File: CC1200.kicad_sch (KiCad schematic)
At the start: 55 parts, among them U3 CC1200, U4 MCP6001-OT, X1 40MHz

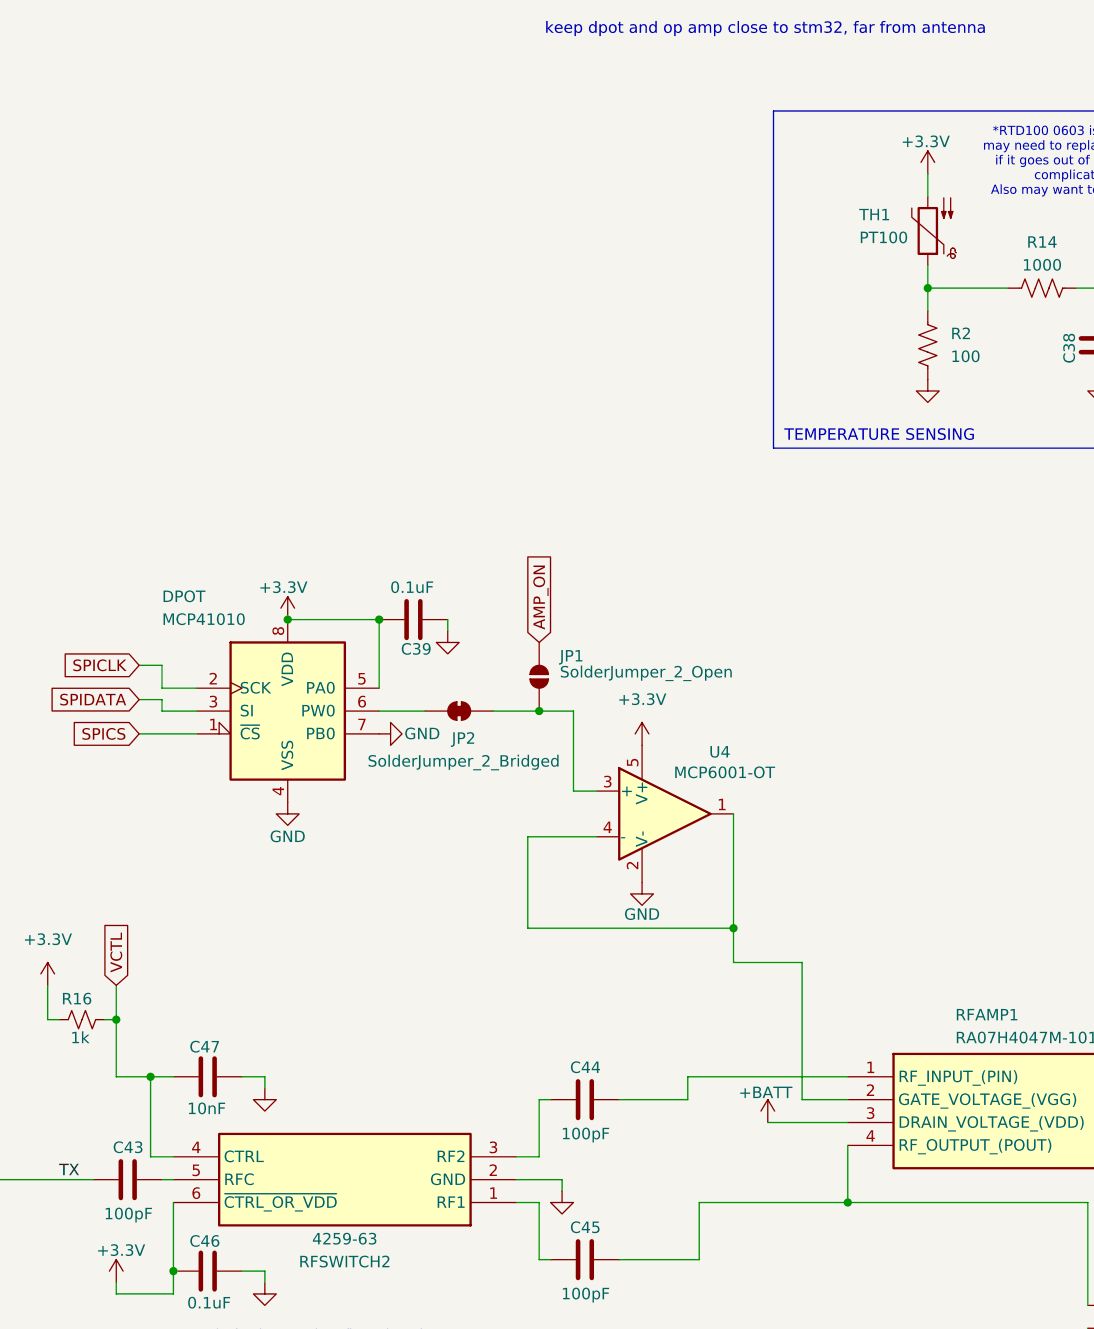
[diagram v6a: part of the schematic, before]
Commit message: reference/backup for mostly routed pcb
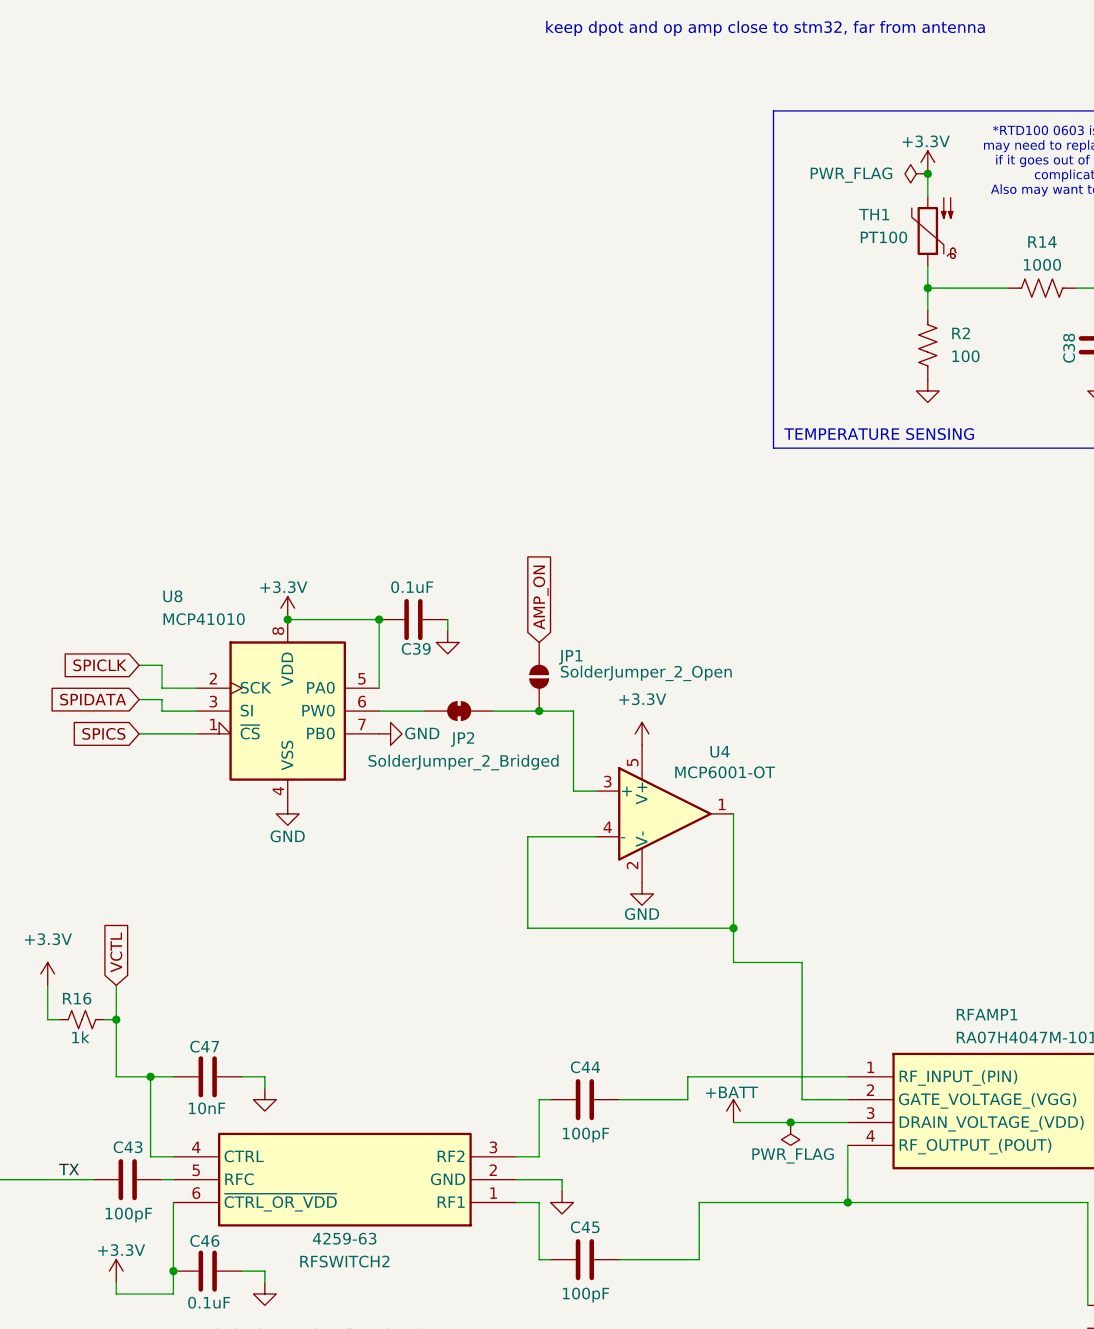
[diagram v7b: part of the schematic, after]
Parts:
- AE1: footprint (none) -> Connector_Coaxial:SMA_BAT_Wireless_BWSMA-KWE-Z001; LCSC (none) -> C7498154
- JP1: footprint (none) -> Jumper:SolderJumper-2_P1.3mm_Open_RoundedPad1.0x1.5mm
- JP2: footprint (none) -> Jumper:SolderJumper-2_P1.3mm_Bridged_RoundedPad1.0x1.5mm
- RFAMP1: footprint RA07H4047M:RA07H4047M101 -> RA07H4047M:RA07H4047M101_HORIZ
- U8: renamed from DPOT; footprint (none) -> MCP41010:SOIC127P599X175-8N; LCSC (none) -> C136395
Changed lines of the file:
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@@
 	)
 	(junction
+		(at 346.71 142.24)
+		(diameter 0)
+		(color 0 0 0 0)
+	)
+	(junction
 		(at 166.37 148.59)
 		(diameter 0)
@@
 	)
 	(junction
+		(at 361.95 36.83)
+		(diameter 0)
+		(color 0 0 0 0)
+	)
+	(junction
 		(at 300.99 86.36)
 		(diameter 0)
@@
 	(wire
 		(pts
-			(xy 344.17 142.24) (xy 353.06 142.24)
+			(xy 340.36 142.24) (xy 346.71 142.24)
 		)
 		(stroke
@@
 	(wire
 		(pts
+			(xy 346.71 142.24) (xy 353.06 142.24)
+		)
+		(stroke
+			(width 0)
+			(type default)
+		)
+	)
+	(wire
+		(pts
 			(xy 228.6 140.97) (xy 228.6 148.59)
 		)
@@
 		(on_board yes)
 		(dnp no)
-		(property "Reference" "DPOT"
+		(property "Reference" "U8"
 			(at 276.86 83.82 0)
 			(effects
@@
 			)
 		)
-		(property "Footprint" ""
+		(property "Footprint" "MCP41010:SOIC127P599X175-8N"
 			(at 290.83 96.52 0)
 			(effects
@@
 			)
 		)
+		(property "LCSC" "C136395"
+			(at 290.83 96.52 0)
+			(effects
+				(font
+					(size 1.27 1.27)
+				)
+				(hide yes)
+			)
+		)
 		(pin "2"
 		)
@@
 			(project ""
 				(path "/4108571e-8c4c-4eba-a51f-04b21c4cec35/dfcafdf4-f213-4518-865d-ab9ee2b88e54"
-					(reference "DPOT")
+					(reference "U8")
 					(unit 1)
 				)
@@
 	)
 	(symbol
+		(lib_id "power:PWR_FLAG")
+		(at 361.95 36.83 90)
+		(unit 1)
+		(exclude_from_sim no)
+		(in_bom yes)
+		(on_board yes)
+		(dnp no)
+		(fields_autoplaced yes)
+		(property "Reference" "#FLG05"
+			(at 360.045 36.83 0)
+			(effects
+				(font
+					(size 1.27 1.27)
+				)
+				(hide yes)
+			)
+		)
+		(property "Value" "PWR_FLAG"
+			(at 358.14 36.8299 90)
+			(effects
+				(font
+					(size 1.27 1.27)
+				)
+				(justify left)
+			)
+		)
+		(property "Footprint" ""
+			(at 361.95 36.83 0)
+			(effects
+				(font
+					(size 1.27 1.27)
+				)
+				(hide yes)
+			)
+		)
+		(property "Datasheet" "~"
+			(at 361.95 36.83 0)
+			(effects
+				(font
+					(size 1.27 1.27)
+				)
+				(hide yes)
+			)
+		)
+		(property "Description" "Special symbol for telling ERC where power comes from"
+			(at 361.95 36.83 0)
+			(effects
+				(font
+					(size 1.27 1.27)
+				)
+				(hide yes)
+			)
+		)
+		(pin "1"
+		)
+		(instances
+			(project ""
+				(path "/4108571e-8c4c-4eba-a51f-04b21c4cec35/dfcafdf4-f213-4518-865d-ab9ee2b88e54"
+					(reference "#FLG05")
+					(unit 1)
+				)
+			)
+		)
+	)
+	(symbol
 		(lib_id "power:GND")
 		(at 125.73 113.03 0)
@@
 	)
 	(symbol
+		(lib_id "power:PWR_FLAG")
+		(at 346.71 142.24 180)
+		(unit 1)
+		(exclude_from_sim no)
+		(in_bom yes)
+		(on_board yes)
+		(dnp no)
+		(property "Reference" "#FLG04"
+			(at 346.71 144.145 0)
+			(effects
+				(font
+					(size 1.27 1.27)
+				)
+				(hide yes)
+			)
+		)
+		(property "Value" "PWR_FLAG"
+			(at 346.964 145.796 0)
+			(effects
+				(font
+					(size 1.27 1.27)
+				)
+			)
+		)
+		(property "Footprint" ""
+			(at 346.71 142.24 0)
+			(effects
+				(font
+					(size 1.27 1.27)
+				)
+				(hide yes)
+			)
+		)
+		(property "Datasheet" "~"
+			(at 346.71 142.24 0)
+			(effects
+				(font
+					(size 1.27 1.27)
+				)
+				(hide yes)
+			)
+		)
+		(property "Description" "Special symbol for telling ERC where power comes from"
+			(at 346.71 142.24 0)
+			(effects
+				(font
+					(size 1.27 1.27)
+				)
+				(hide yes)
+			)
+		)
+		(pin "1"
+		)
+		(instances
+			(project ""
+				(path "/4108571e-8c4c-4eba-a51f-04b21c4cec35/dfcafdf4-f213-4518-865d-ab9ee2b88e54"
+					(reference "#FLG04")
+					(unit 1)
+				)
+			)
+		)
+	)
+	(symbol
 		(lib_id "power:GND")
 		(at 168.91 91.44 0)
@@
 			)
 		)
-		(property "Footprint" "RA07H4047M:RA07H4047M101"
+		(property "Footprint" "RA07H4047M:RA07H4047M101_HORIZ"
 			(at 392.43 232.08 0)
 			(effects
@@
 			)
 		)
-		(property "Footprint" ""
+		(property "Footprint" "Jumper:SolderJumper-2_P1.3mm_Bridged_RoundedPad1.0x1.5mm"
 			(at 309.88 96.52 0)
 			(effects
@@
 			)
 		)
-		(property "Footprint" ""
+		(property "Footprint" "Connector_Coaxial:SMA_BAT_Wireless_BWSMA-KWE-Z001"
 			(at 387.35 162.56 0)
 			(effects
@@
 			)
 		)
-		(property "Datasheet" "~"
+		(property "Datasheet" "https://jlcpcb.com/api/file/downloadByFileSystemAccessId/8600772178468225024"
 			(at 387.35 162.56 0)
 			(effects
@@
 			)
 		)
+		(property "LCSC" "C7498154"
+			(at 384.81 162.56 90)
+			(effects
+				(font
+					(size 1.27 1.27)
+				)
+				(hide yes)
+			)
+		)
 		(pin "1"
 		)
@@
 			)
 		)
-		(property "Footprint" ""
+		(property "Footprint" "Jumper:SolderJumper-2_P1.3mm_Open_RoundedPad1.0x1.5mm"
 			(at 318.77 92.71 0)
 			(effects
@@
 	(symbol
 		(lib_id "power:+BATT")
-		(at 344.17 142.24 0)
+		(at 340.36 142.24 0)
 		(unit 1)
 		(exclude_from_sim no)
@@
 		(dnp no)
 		(property "Reference" "#PWR04"
-			(at 344.17 146.05 0)
+			(at 340.36 146.05 0)
 			(effects
 				(font
@@
 		)
 		(property "Value" "+BATT"
-			(at 343.916 138.938 0)
+			(at 340.106 138.938 0)
 			(effects
 				(font
@@
 		)
 		(property "Footprint" ""
-			(at 344.17 142.24 0)
+			(at 340.36 142.24 0)
 			(effects
 				(font
@@
 		)
 		(property "Datasheet" ""
-			(at 344.17 142.24 0)
+			(at 340.36 142.24 0)
 			(effects
 				(font
@@
 		)
 		(property "Description" "Power symbol creates a global label with name \"+BATT\""
-			(at 344.17 142.24 0)
+			(at 340.36 142.24 0)
 			(effects
 				(font

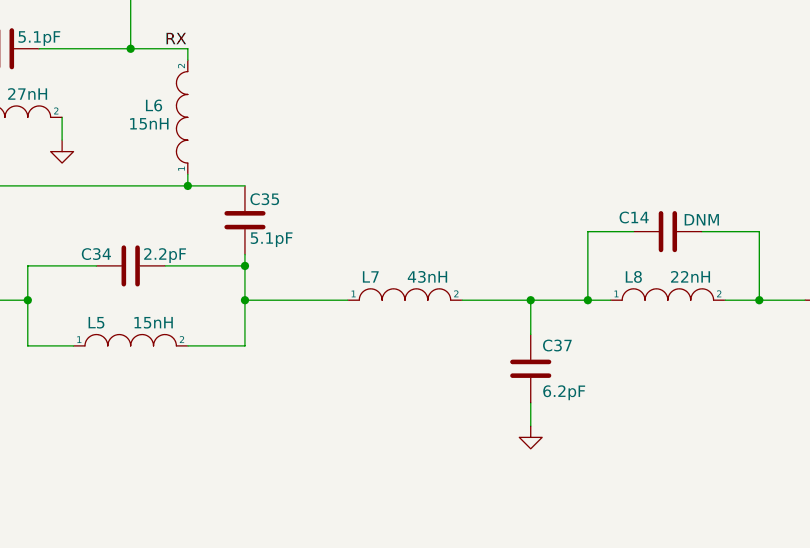
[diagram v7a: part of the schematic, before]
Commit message: finished routing pcb and passed DRC, waiting for review by Ethan
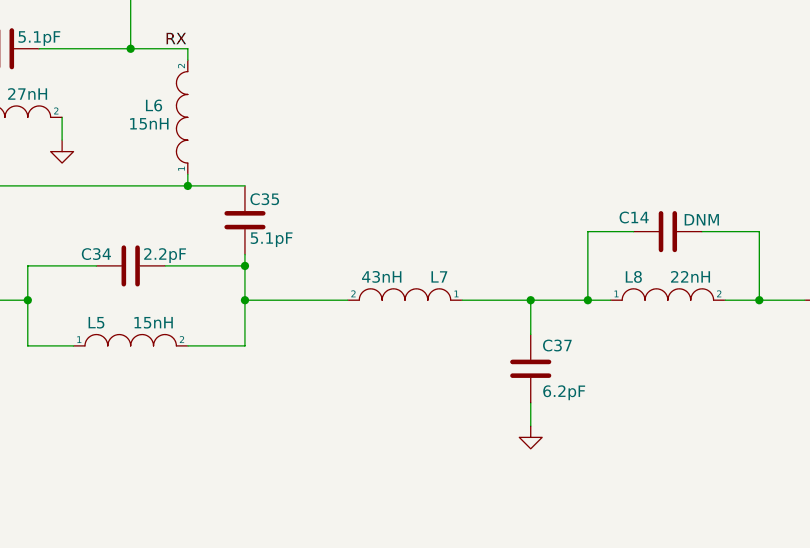
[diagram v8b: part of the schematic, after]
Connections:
- net at C34.1, C35.2, L5.2: now also L7.2; no longer L7.1
- net at C14.1, C37.1, L8.1: now also L7.1; no longer L7.2
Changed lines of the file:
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@@
 		(lib_id "pspice:INDUCTOR")
 		(at 208.28 148.59 0)
+		(mirror y)
 		(unit 1)
 		(exclude_from_sim no)
@@
 		(dnp no)
 		(property "Reference" "L7"
-			(at 204.47 146.05 0)
+			(at 212.09 146.05 0)
 			(effects
 				(font
@@
 		)
 		(property "Value" "43nH"
-			(at 210.82 146.05 0)
+			(at 205.74 146.05 0)
 			(effects
 				(font
